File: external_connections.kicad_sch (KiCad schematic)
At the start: 9 parts, among them J1 PWR IN, J2 EXT_CLK_IN5, J3 PWR Test, U1 PTLV709A33DBVR

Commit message: printed pdf from schematics
Signed-off-by: Mika Laitio <lamikr@gmail.com>
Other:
- company: (none) -> Mika Laitio
- title: (none) -> I2S Audio to AES/EBU Optical Toslink
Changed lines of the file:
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@@
   (paper "A4")
   (title_block
+    (title "I2S Audio to AES/EBU Optical Toslink")
     (date "2023-12-26")
     (rev "v0.1")
+    (company "Mika Laitio")
   )
   (junction (at 100.965 80.01) (diameter 0) (color 0 0 0 0)

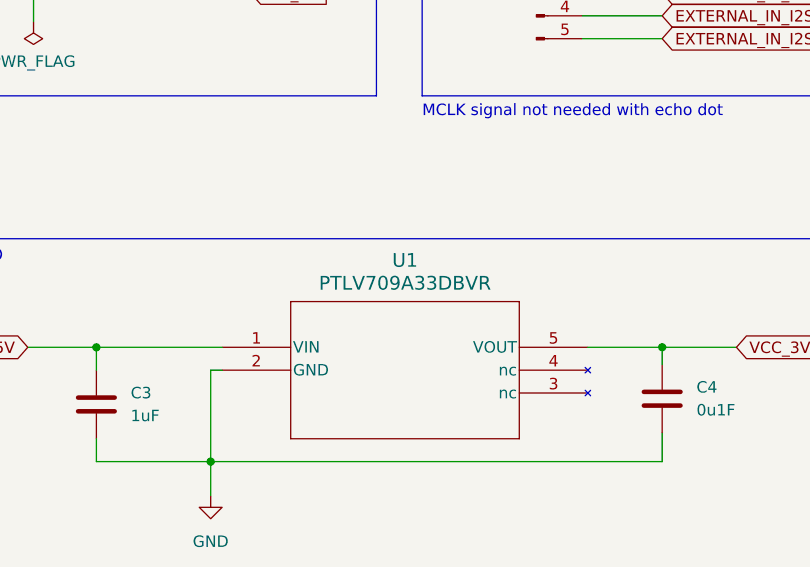
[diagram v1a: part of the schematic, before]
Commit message: added mpn and sku_digikey numbers for bom
Signed-off-by: Mika Laitio <lamikr@gmail.com>
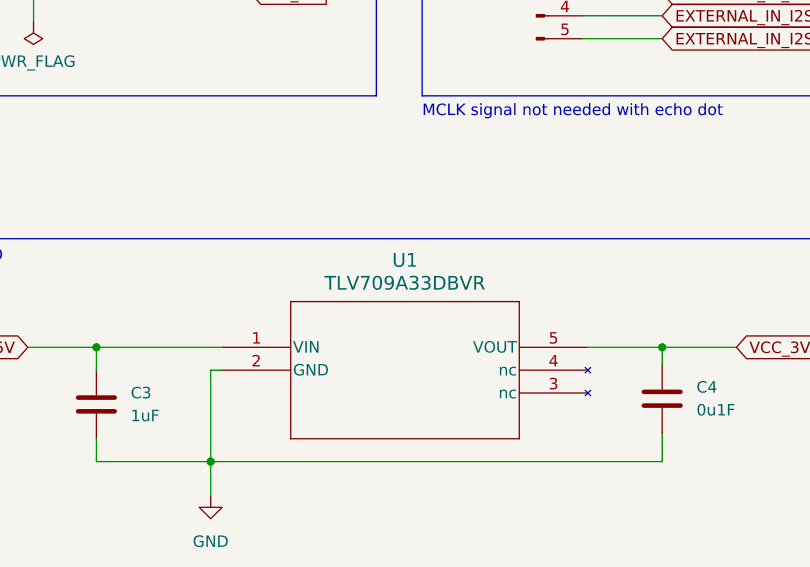
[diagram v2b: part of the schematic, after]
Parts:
- C1: MFR (none) -> Murata; MPN (none) -> GRM155R60J475ME47D; SKU_DIGIKEY (none) -> 490-5915-1-ND
- C2, C4, C5: MFR (none) -> Murata; MPN (none) -> GRM033R61A104ME15D; SKU_DIGIKEY (none) -> 490-5405-1-ND
- C3: MFR (none) -> Murata; MPN (none) -> GRM155R70J105KA12J; SKU_DIGIKEY (none) -> 490-13339-1-ND
- J3: MFR (none) -> Würth Elektronik; MPN (none) -> 61300311121; Price (none) -> 0.13; SKU_DIGIKEY (none) -> 732-5316-ND
- U1: value PTLV709A33DBVR -> TLV709A33DBVR; MFR (none) -> TI; MPN (none) -> TLV709A33DBVR; Price (none) -> 0.76; SKU_DIGIKEY (none) -> 296-TLV709A33DBVRTR-ND
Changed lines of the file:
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@@
+      (effects (font (size 1.27 1.27)) hide)
+    )
+    (property "MFR" "Würth Elektronik" (at 149.86 38.1 0)
+      (effects (font (size 1.27 1.27)) hide)
+    )
+    (property "MPN" "61300311121" (at 149.86 38.1 0)
+      (effects (font (size 1.27 1.27)) hide)
+    )
+    (property "Notes" "" (at 149.86 38.1 0)
+      (effects (font (size 1.27 1.27)) hide)
+    )
+    (property "Price" "0.13" (at 149.86 38.1 0)
+      (effects (font (size 1.27 1.27)) hide)
+    )
+    (property "SKU_DIGIKEY" "732-5316-ND" (at 149.86 38.1 0)
       (effects (font (size 1.27 1.27)) hide)
     )
@@
       (effects (font (size 1.524 1.524)))
     )
-    (property "Value" "PTLV709A33DBVR" (at 72.39 72.898 0)
+    (property "Value" "TLV709A33DBVR" (at 72.39 72.898 0)
       (effects (font (size 1.524 1.524)))
     )
@@
       (effects (font (size 1.27 1.27) italic) hide)
     )
-    (property "Datasheet" "PTLV709A33DBVR" (at 52.07 80.01 0)
+    (property "Datasheet" "" (at 52.07 80.01 0)
       (effects (font (size 1.27 1.27) italic) hide)
+    )
+    (property "Notes" "" (at 52.07 80.01 0)
+      (effects (font (size 1.27 1.27)) hide)
+    )
+    (property "Price" "0.76" (at 52.07 80.01 0)
+      (effects (font (size 1.27 1.27)) hide)
+    )
+    (property "MFR" "TI" (at 52.07 80.01 0)
+      (effects (font (size 1.27 1.27)) hide)
+    )
+    (property "MPN" "TLV709A33DBVR" (at 52.07 80.01 0)
+      (effects (font (size 1.27 1.27)) hide)
+    )
+    (property "SKU_DIGIKEY" "296-TLV709A33DBVRTR-ND" (at 52.07 80.01 0)
+      (effects (font (size 1.27 1.27)) hide)
     )
     (pin "4")
@@
       (effects (font (size 1.27 1.27)) hide)
     )
+    (property "Notes" "" (at 86.995 40.64 0)
+      (effects (font (size 1.27 1.27)) hide)
+    )
+    (property "Price" "" (at 86.995 40.64 0)
+      (effects (font (size 1.27 1.27)) hide)
+    )
     (pin "2")
     (pin "4")
@@
       (effects (font (size 1.27 1.27)) hide)
     )
+    (property "Notes" "" (at 38.1 86.36 0)
+      (effects (font (size 1.27 1.27)) hide)
+    )
+    (property "Price" "" (at 38.1 86.36 0)
+      (effects (font (size 1.27 1.27)) hide)
+    )
+    (property "MFR" "Murata" (at 38.1 86.36 0)
+      (effects (font (size 1.27 1.27)) hide)
+    )
+    (property "MPN" "GRM155R70J105KA12J" (at 38.1 86.36 0)
+      (effects (font (size 1.27 1.27)) hide)
+    )
+    (property "SKU_DIGIKEY" "490-13339-1-ND" (at 38.1 86.36 0)
+      (effects (font (size 1.27 1.27)) hide)
+    )
     (pin "2")
     (pin "1")
@@
       (effects (font (size 1.27 1.27)) hide)
     )
+    (property "Notes" "" (at 22.225 38.1 0)
+      (effects (font (size 1.27 1.27)) hide)
+    )
+    (property "Price" "" (at 22.225 38.1 0)
+      (effects (font (size 1.27 1.27)) hide)
+    )
     (pin "2")
     (pin "1")
@@
       (effects (font (size 1.27 1.27)) hide)
     )
+    (property "Notes" "" (at 46.355 35.56 0)
+      (effects (font (size 1.27 1.27)) hide)
+    )
+    (property "Price" "" (at 46.355 35.56 0)
+      (effects (font (size 1.27 1.27)) hide)
+    )
+    (property "MFR" "Murata" (at 46.355 35.56 0)
+      (effects (font (size 1.27 1.27)) hide)
+    )
+    (property "MPN" "GRM033R61A104ME15D" (at 46.355 35.56 0)
+      (effects (font (size 1.27 1.27)) hide)
+    )
+    (property "SKU_DIGIKEY" "490-5405-1-ND " (at 46.355 35.56 0)
+      (effects (font (size 1.27 1.27)) hide)
+    )
     (pin "1")
     (pin "2")
@@
       (effects (font (size 1.27 1.27)) hide)
     )
+    (property "Notes" "" (at 33.655 35.56 0)
+      (effects (font (size 1.27 1.27)) hide)
+    )
+    (property "Price" "" (at 33.655 35.56 0)
+      (effects (font (size 1.27 1.27)) hide)
+    )
+    (property "MFR" "Murata" (at 33.655 35.56 0)
+      (effects (font (size 1.27 1.27)) hide)
+    )
+    (property "MPN" "GRM155R60J475ME47D" (at 33.655 35.56 0)
+      (effects (font (size 1.27 1.27)) hide)
+    )
+    (property "SKU_DIGIKEY" "490-5915-1-ND" (at 33.655 35.56 0)
+      (effects (font (size 1.27 1.27)) hide)
+    )
     (pin "1")
     (pin "2")
@@
       (effects (font (size 1.27 1.27)) hide)
     )
+    (property "Notes" "" (at 100.965 85.725 0)
+      (effects (font (size 1.27 1.27)) hide)
+    )
+    (property "Price" "" (at 100.965 85.725 0)
+      (effects (font (size 1.27 1.27)) hide)
+    )
+    (property "MFR" "Murata" (at 100.965 85.725 0)
+      (effects (font (size 1.27 1.27)) hide)
+    )
+    (property "MPN" "GRM033R61A104ME15D" (at 100.965 85.725 0)
+      (effects (font (size 1.27 1.27)) hide)
+    )
+    (property "SKU_DIGIKEY" "490-5405-1-ND " (at 100.965 85.725 0)
+      (effects (font (size 1.27 1.27)) hide)
+    )
     (pin "2")
     (pin "1")
@@
       (effects (font (size 1.27 1.27)) hide)
     )
+    (property "Notes" "" (at 161.29 33.02 0)
+      (effects (font (size 1.27 1.27)) hide)
+    )
+    (property "Price" "" (at 161.29 33.02 0)
+      (effects (font (size 1.27 1.27)) hide)
+    )
+    (property "MFR" "Murata" (at 161.29 33.02 0)
+      (effects (font (size 1.27 1.27)) hide)
+    )
+    (property "MPN" "GRM033R61A104ME15D" (at 161.29 33.02 0)
+      (effects (font (size 1.27 1.27)) hide)
+    )
+    (property "SKU_DIGIKEY" "490-5405-1-ND " (at 161.29 33.02 0)
+      (effects (font (size 1.27 1.27)) hide)
+    )

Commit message: optimized bom from digikey
Signed-off-by: Mika Laitio <lamikr@gmail.com>
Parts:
- C1, C2, C3, C4, C5: QtyOrdered (none) -> 100
- J3: QtyOrdered (none) -> 25
- U1: QtyOrdered (none) -> 10; SKU_DIGIKEY 296-TLV709A33DBVRTR-ND -> 296-TLV709A33DBVRDKR-ND
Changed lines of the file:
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@@
+      (effects (font (size 1.27 1.27)) hide)
+    )
+    (property "QtyOrdered" "25" (at 149.86 38.1 0)
       (effects (font (size 1.27 1.27)) hide)
     )
@@
       (effects (font (size 1.27 1.27) italic) hide)
     )
-    (property "Datasheet" "" (at 52.07 80.01 0)
+    (property "Datasheet" "~" (at 52.07 80.01 0)
       (effects (font (size 1.27 1.27) italic) hide)
     )
@@
       (effects (font (size 1.27 1.27)) hide)
     )
-    (property "SKU_DIGIKEY" "296-TLV709A33DBVRTR-ND" (at 52.07 80.01 0)
+    (property "SKU_DIGIKEY" "296-TLV709A33DBVRDKR-ND" (at 52.07 80.01 0)
+      (effects (font (size 1.27 1.27)) hide)
+    )
+    (property "QtyOrdered" "10" (at 52.07 80.01 0)
       (effects (font (size 1.27 1.27)) hide)
     )
@@
       (effects (font (size 1.27 1.27)) hide)
     )
+    (property "QtyOrdered" "" (at 86.995 40.64 0)
+      (effects (font (size 1.27 1.27)) hide)
+    )
     (pin "2")
     (pin "4")
@@
       (effects (font (size 1.27 1.27)) hide)
     )
+    (property "QtyOrdered" "100" (at 38.1 86.36 0)
+      (effects (font (size 1.27 1.27)) hide)
+    )
     (pin "2")
     (pin "1")
@@
       (effects (font (size 1.27 1.27)) hide)
     )
+    (property "QtyOrdered" "" (at 22.225 38.1 0)
+      (effects (font (size 1.27 1.27)) hide)
+    )
     (pin "2")
     (pin "1")
@@
       (effects (font (size 1.27 1.27)) hide)
     )
+    (property "QtyOrdered" "100" (at 46.355 35.56 0)
+      (effects (font (size 1.27 1.27)) hide)
+    )
     (pin "1")
     (pin "2")
@@
       (effects (font (size 1.27 1.27)) hide)
     )
+    (property "QtyOrdered" "100" (at 33.655 35.56 0)
+      (effects (font (size 1.27 1.27)) hide)
+    )
     (pin "1")
     (pin "2")
@@
       (effects (font (size 1.27 1.27)) hide)
     )
+    (property "QtyOrdered" "100" (at 100.965 85.725 0)
+      (effects (font (size 1.27 1.27)) hide)
+    )
     (pin "2")
     (pin "1")
@@
       (effects (font (size 1.27 1.27)) hide)
     )
+    (property "QtyOrdered" "100" (at 161.29 33.02 0)
+      (effects (font (size 1.27 1.27)) hide)
+    )

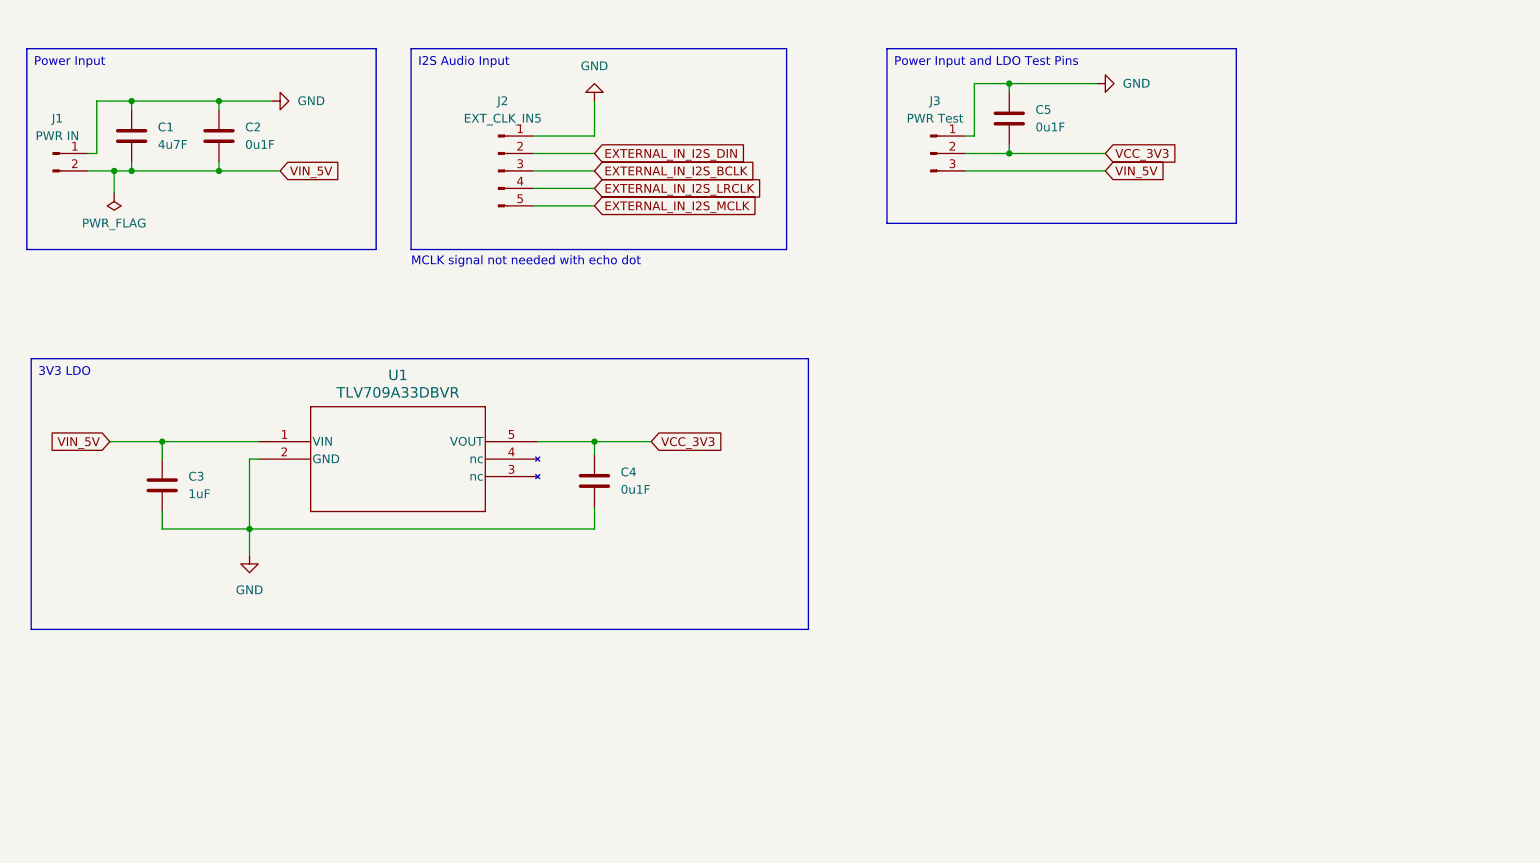
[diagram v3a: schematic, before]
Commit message: various updates
- removed duplicates 5V power connectors
- now the whole pcb is always powered via 6 pin
  atmega avr isp connector
- added connector for wm8805 rx0 and rx1
- added labels for jumpers/connectors
- moved the orientation of existing connecors
- moved the location of ldo close to
  6 pin avr isp connector

Signed-off-by: Mika Laitio <lamikr@gmail.com>
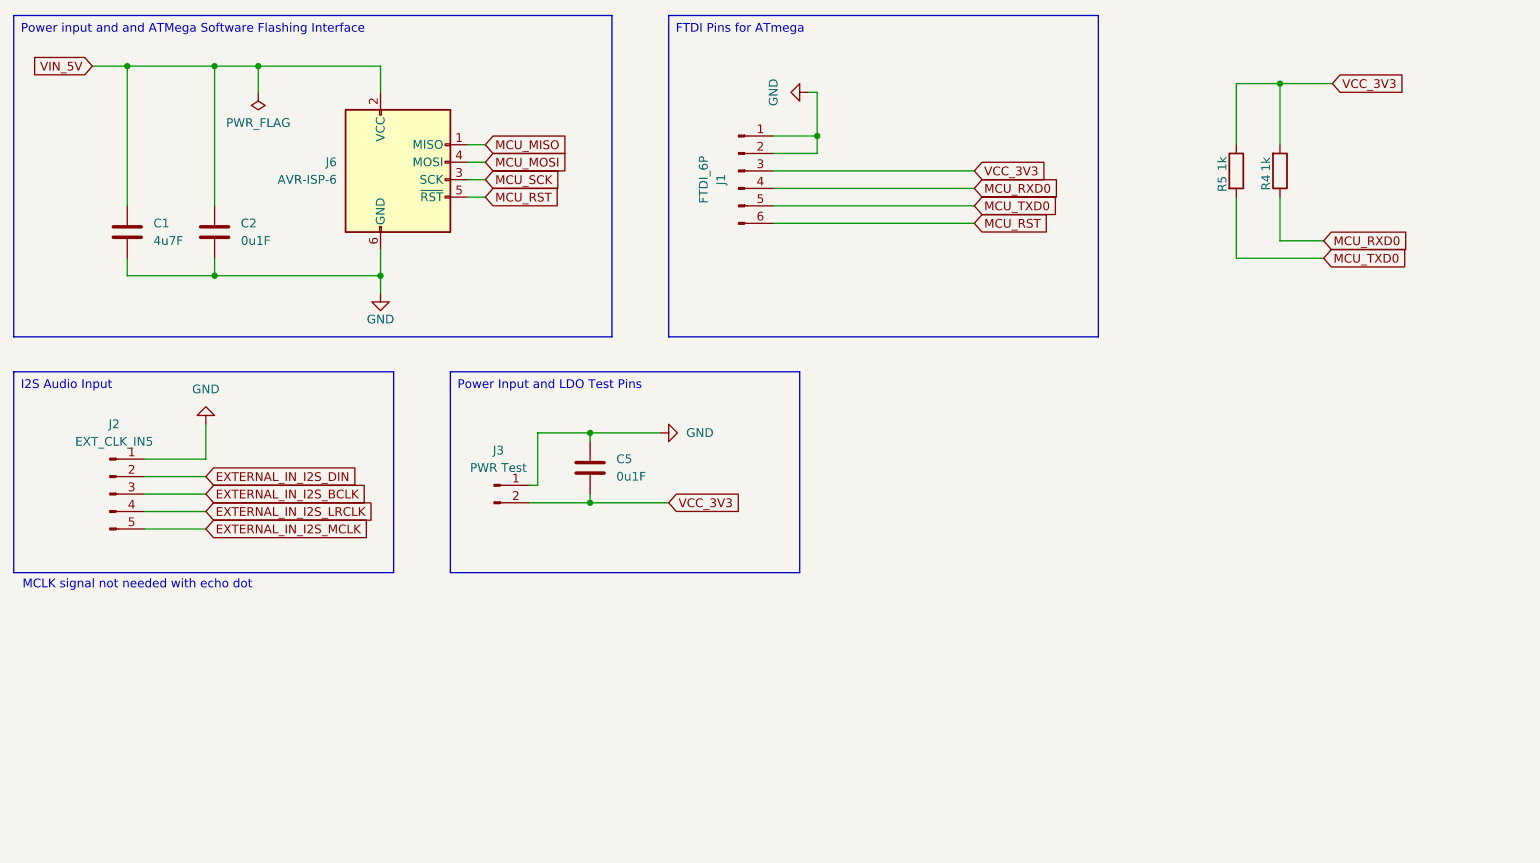
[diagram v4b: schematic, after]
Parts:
- removed C3: 1uF, Capacitor_SMD:C_0402_1005Metric, symbol Device:C
- removed C4: 0u1F, Capacitor_SMD:C_0402_1005Metric, symbol Device:C
- removed J1: PWR IN, Connector_PinHeader_2.54mm:PinHeader_1x02_P2.54mm_Vertical, symbol Connector:Conn_01x02_Pin
- removed U1: TLV709A33DBVR, SOT-23-5_DBV_TEX, symbol lamikr_tlv709:PTLV709A33DBVR
- added J1: FTDI_6P, Connector_PinHeader_2.54mm:PinHeader_1x06_P2.54mm_Vertical, symbol Connector:Conn_01x06_Pin
- added J6: AVR-ISP-6, Connector_PinHeader_2.54mm:PinHeader_2x03_P2.54mm_Vertical, symbol Connector:AVR-ISP-6
- added R4, R5: 1k, Resistor_SMD:R_0402_1005Metric, symbol Device:R
- J3: footprint Connector_PinHeader_2.54mm:PinHeader_1x03_P2.54mm_Vertical -> Connector_PinHeader_2.54mm:PinHeader_1x02_P2.54mm_Vertical; symbol Connector:Conn_01x03_Pin -> Connector:Conn_01x02_Pin
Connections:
- net GND: now also C1.2, C2.2, J1.1 (Pin_1), J1.2 (Pin_2), J6.6 (GND); no longer C1.1, C2.1
- net VCC_3V3: now also J1.3 (Pin_3), R4.2, R5.1
- net VIN_5V: now also C1.1, C2.1, J6.2 (VCC); no longer C1.2, C2.2, J3.3 (Pin_3)
- new net MCU_MISO: J6.1 (MISO)
- new net MCU_MOSI: J6.4 (MOSI)
- new net MCU_RST: J1.6 (Pin_6), J6.5 (~{RST})
- new net MCU_RXD0: J1.4 (Pin_4), R4.1
- new net MCU_SCK: J6.3 (SCK)
- new net MCU_TXD0: J1.5 (Pin_5), R5.2
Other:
- moved on the sheet: C1, C2, C5, J2

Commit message: finished v0.2 design
- mcu ftdi serial connector reset pin
  to 3v3 instead of 5v
- 3.3v pull-up resistor, cap and diode for mcu reset
- mcu reset button
- solder paste clearance -20% for
  mcu, codec, clk gen and ldo to help
  spreading pasta to small pins close to
  ech others

Signed-off-by: Mika Laitio <lamikr@gmail.com>
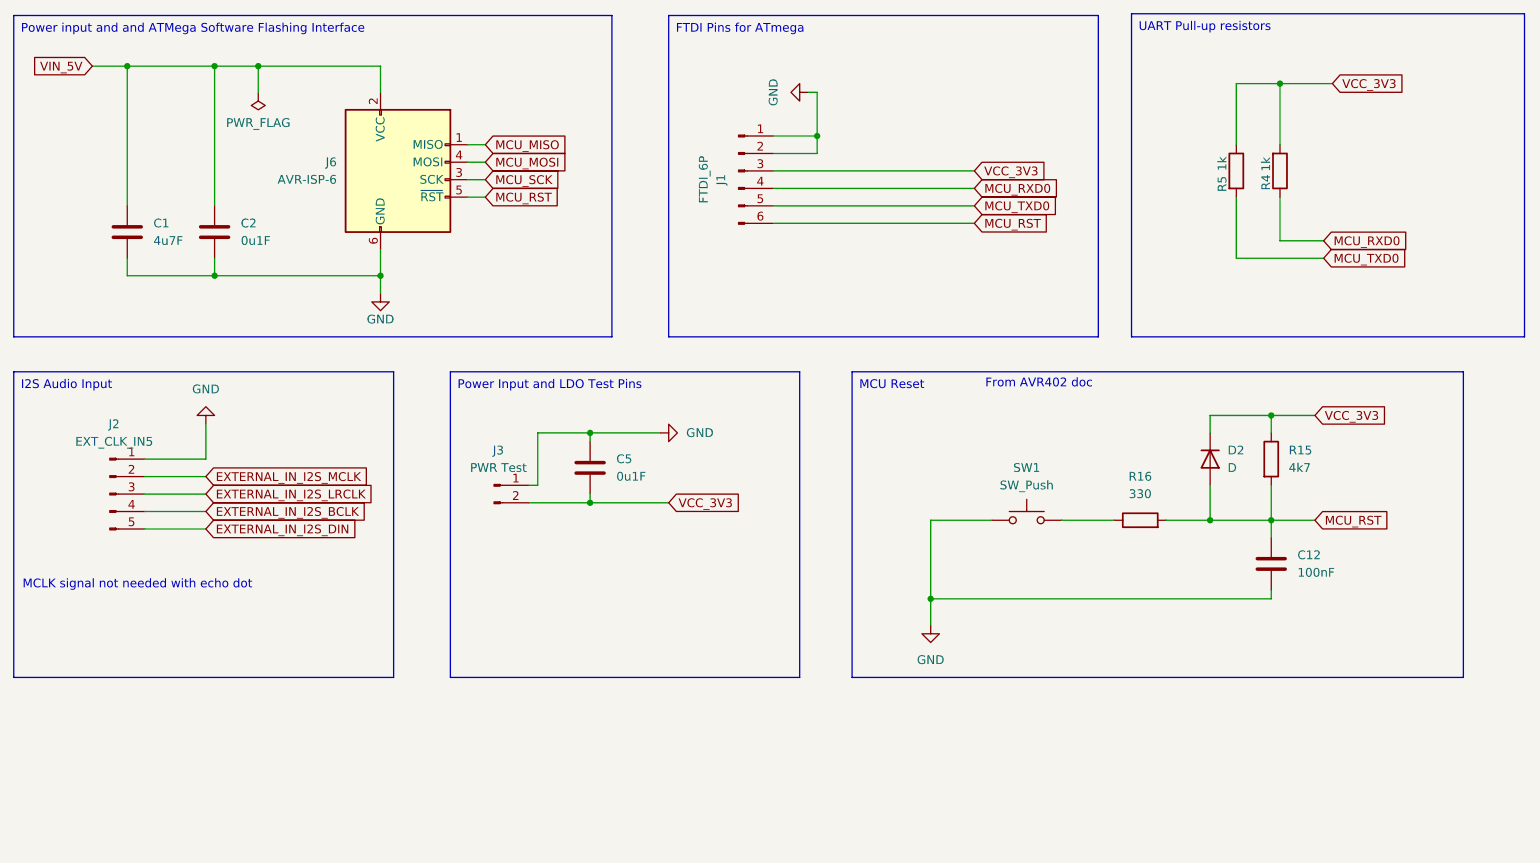
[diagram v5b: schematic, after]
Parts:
- added C12: 100nF, Capacitor_SMD:C_0402_1005Metric, symbol Device:C
- added D2: D, Diode_SMD:D_0402_1005Metric, symbol Device:D
- added R15: 4k7, Resistor_SMD:R_0402_1005Metric, symbol Device:R
- added R16: 330, Resistor_SMD:R_0402_1005Metric, symbol Device:R
- added SW1: SW_Push, Connector_PinHeader_2.54mm:PinHeader_1x02_P2.54mm_Vertical, symbol Switch:SW_Push
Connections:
- net EXTERNAL_IN_I2S_BCLK: now also J2.4 (Pin_4); no longer J2.3 (Pin_3)
- net EXTERNAL_IN_I2S_DIN: now also J2.5 (Pin_5); no longer J2.2 (Pin_2)
- net EXTERNAL_IN_I2S_LRCLK: now also J2.3 (Pin_3); no longer J2.4 (Pin_4)
- net EXTERNAL_IN_I2S_MCLK: now also J2.2 (Pin_2); no longer J2.5 (Pin_5)
- net GND: now also C12.2, SW1.1
- net MCU_RST: now also C12.1, D2.2 (A), R15.2, R16.2
- net VCC_3V3: now also D2.1 (K), R15.1
- new net: R16.1, SW1.2
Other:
- note added: "From AVR402 doc"
